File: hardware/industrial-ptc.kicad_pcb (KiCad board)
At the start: 2 copper layers, 40 x 40 mm, 35 parts, among them P1 CON-SENSOR, P2 Debug, P3 Boot, P4 CONN_01X08, SW1 SW_DIP_4, SW2 SW_DIP_4, U1 XMC1100, U2 MAX31865, U3 DRILL, U4 DRILL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

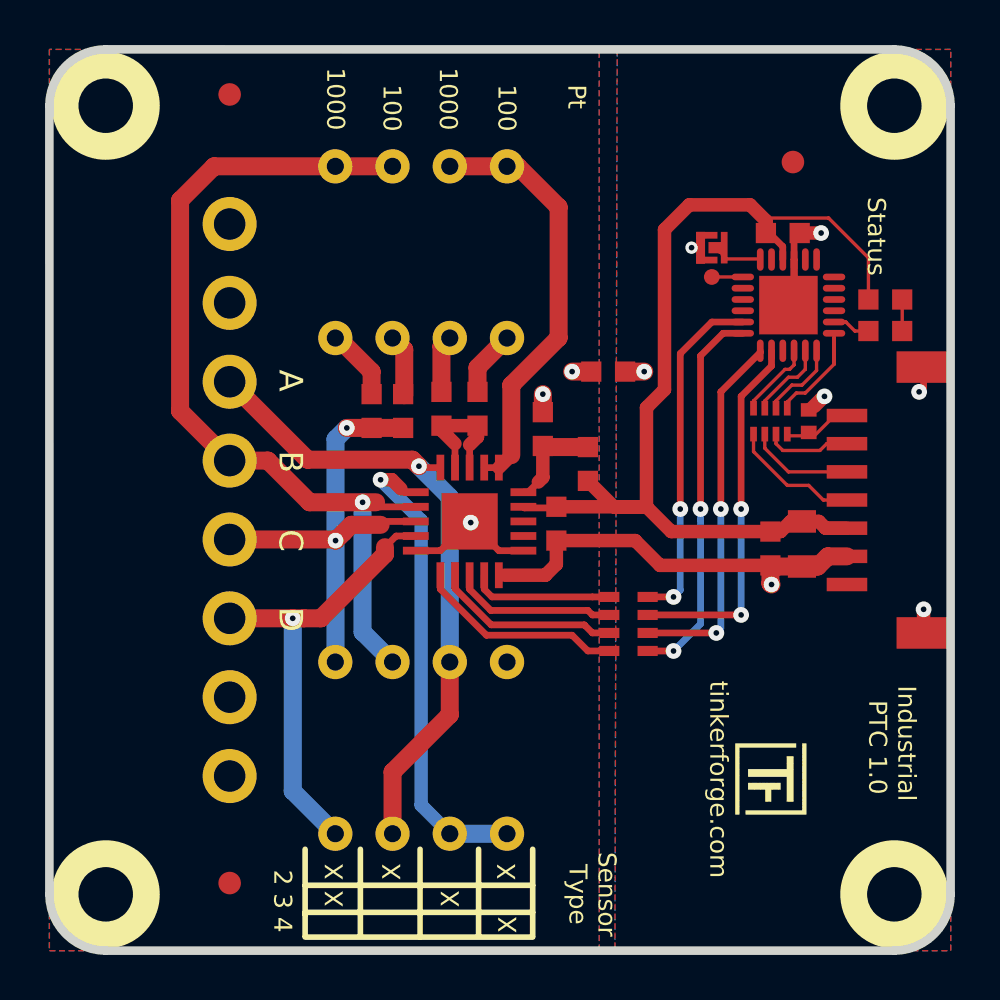
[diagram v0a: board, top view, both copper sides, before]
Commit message: Hardware: Updated files to Kicad 6, added 10MOhm resistor for better disconnect detection
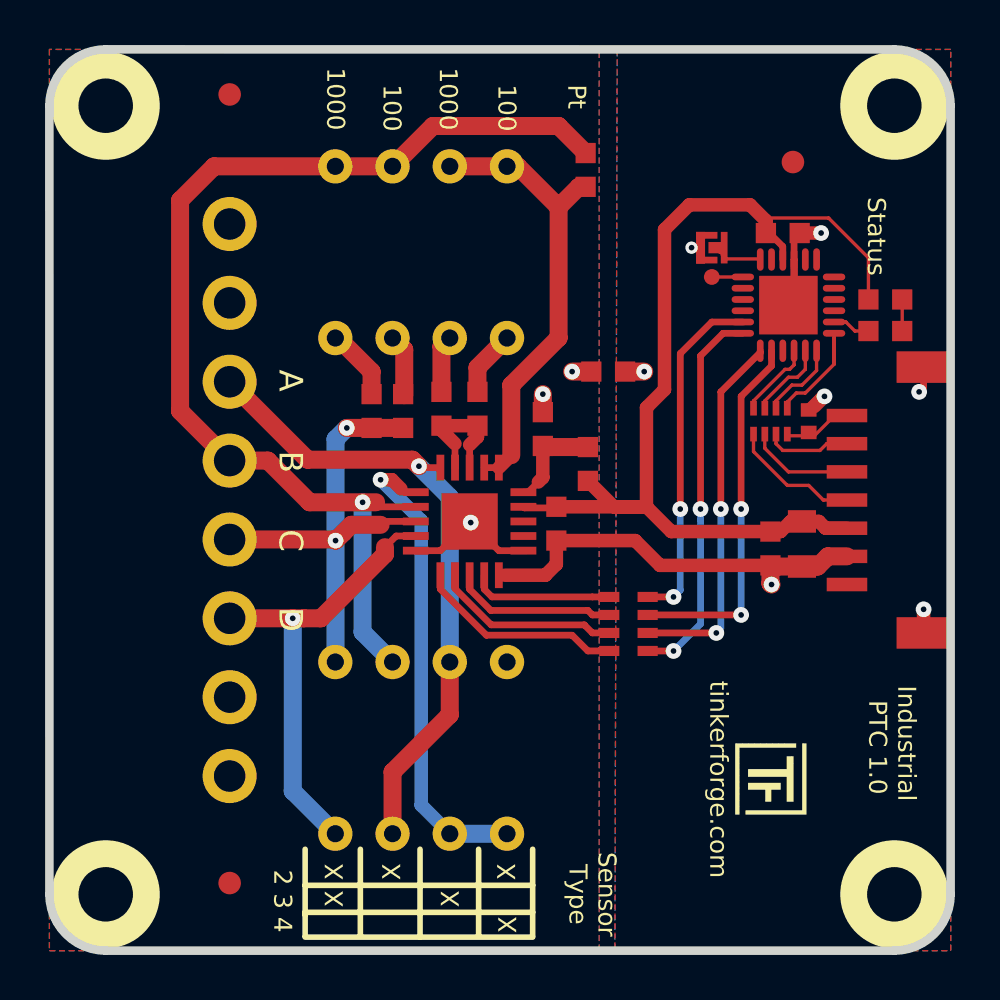
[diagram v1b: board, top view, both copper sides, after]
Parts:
- added R4: 10M, kicad-libraries:R0603F, F.Cu at (148.7, 75.3)
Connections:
- P1 pad 1: Net-(P1-Pad1) -> unconnected-(P1-Pad1)
- U1 pad 11: Net-(U1-Pad11) -> unconnected-(U1-Pad11)
- U1 pad 14: Net-(U1-Pad14) -> unconnected-(U1-Pad14)
- U1 pad 15: Net-(U1-Pad15) -> unconnected-(U1-Pad15)
- U1 pad 16: Net-(U1-Pad16) -> unconnected-(U1-Pad16)
- U1 pad 21: Net-(U1-Pad21) -> unconnected-(U1-Pad21)
- U1 pad 3: Net-(U1-Pad3) -> unconnected-(U1-Pad3)
- U1 pad 4: Net-(U1-Pad4) -> unconnected-(U1-Pad4)
- U1 pad 5: Net-(U1-Pad5) -> unconnected-(U1-Pad5)
- U1 pad 6: Net-(U1-Pad6) -> unconnected-(U1-Pad6)
- U1 pad 7: Net-(U1-Pad7) -> unconnected-(U1-Pad7)
- U1 pad 8: Net-(U1-Pad8) -> unconnected-(U1-Pad8)
- U2 pad 17: Net-(U2-Pad17) -> unconnected-(U2-Pad17)
- U2 pad 18: Net-(U2-Pad18) -> unconnected-(U2-Pad18)
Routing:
- net RTDIN+: track 39.3 -> 49.1 mm
- net Net-(R4-Pad1): track 18.9 -> 20.5 mm
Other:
- net class Default removed

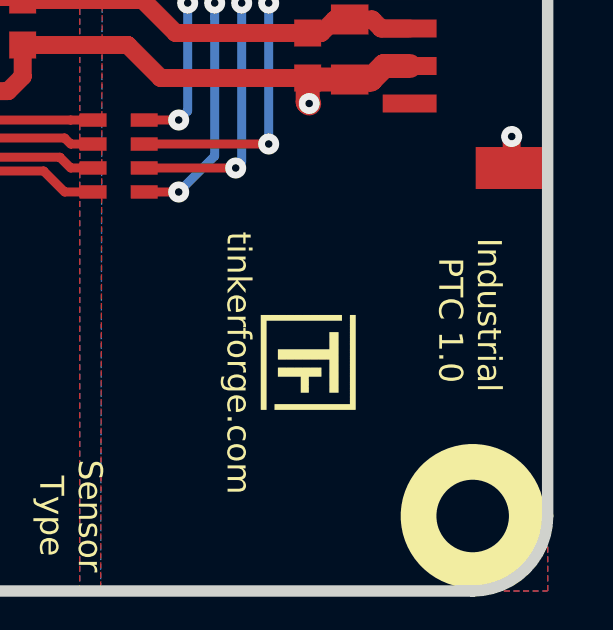
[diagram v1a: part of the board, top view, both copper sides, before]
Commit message: Hardware: changed the silkscreen from to 1.1
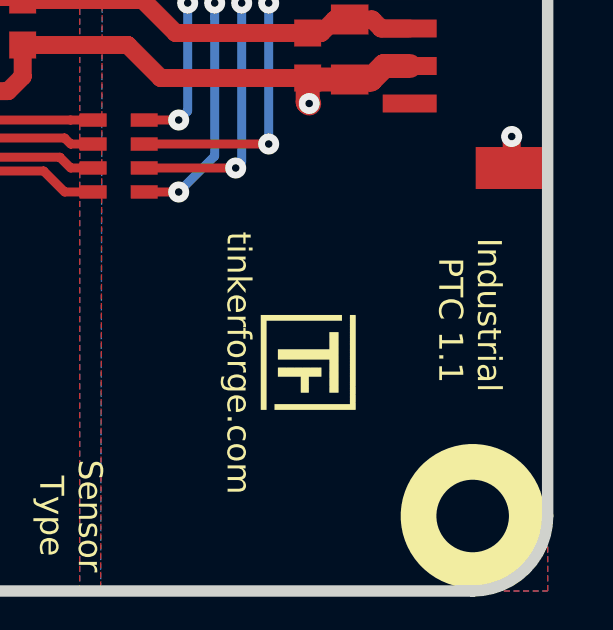
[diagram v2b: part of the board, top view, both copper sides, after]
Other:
- board text added: "Industrial PTC 1.1"
- board text removed: "Industrial PTC 1.0"
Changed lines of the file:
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@@
     (effects (font (size 0.8 0.8) (thickness 0.15)))
   )
-  (gr_text "Industrial\n PTC 1.0" (at 162.3 100.75 270) (layer "F.SilkS")
+  (gr_text "Industrial\n PTC 1.1" (at 162.3 100.75 270) (layer "F.SilkS")
     (effects (font (size 0.8001 0.8001) (thickness 0.14986)))
   )
